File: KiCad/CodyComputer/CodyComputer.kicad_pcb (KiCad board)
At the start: 2 copper layers, 160 x 100 mm, 59 parts, among them J1 Barrel_Jack, J2 Power LED, J3 PropPlug, J4 Video Out, J5 Audio Out, J6 Cody Expansion/Cartridge Port, J7 Keyboard Connector, J8 Joystick 1, J9 Joystick 2, U1 74HC541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

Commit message: Change socket footprints to long pads
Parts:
- U1: footprint Package_DIP:DIP-20_W7.62mm_Socket -> Package_DIP:DIP-20_W7.62mm_Socket_LongPads
- U3, U5, U7: footprint Package_DIP:DIP-40_W15.24mm_Socket -> Package_DIP:DIP-40_W15.24mm_Socket_LongPads
- U4: footprint Package_DIP:DIP-8_W7.62mm_Socket -> Package_DIP:DIP-8_W7.62mm_Socket_LongPads
- U6: footprint Package_DIP:DIP-32_W15.24mm_Socket -> Package_DIP:DIP-32_W15.24mm_Socket_LongPads
- U8: footprint Package_DIP:DIP-16_W7.62mm_Socket -> Package_DIP:DIP-16_W7.62mm_Socket_LongPads

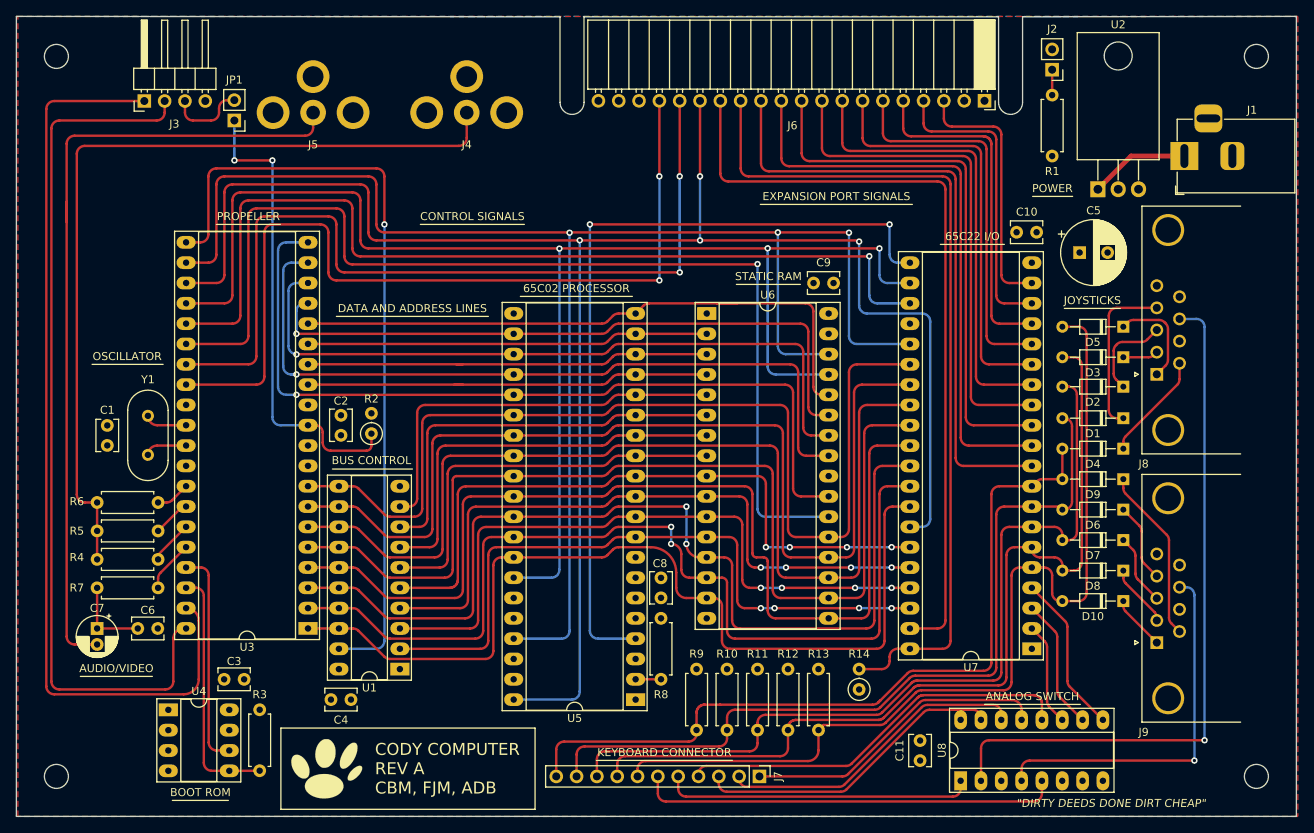
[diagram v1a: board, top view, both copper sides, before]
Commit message: Fix DRC errors for long pads
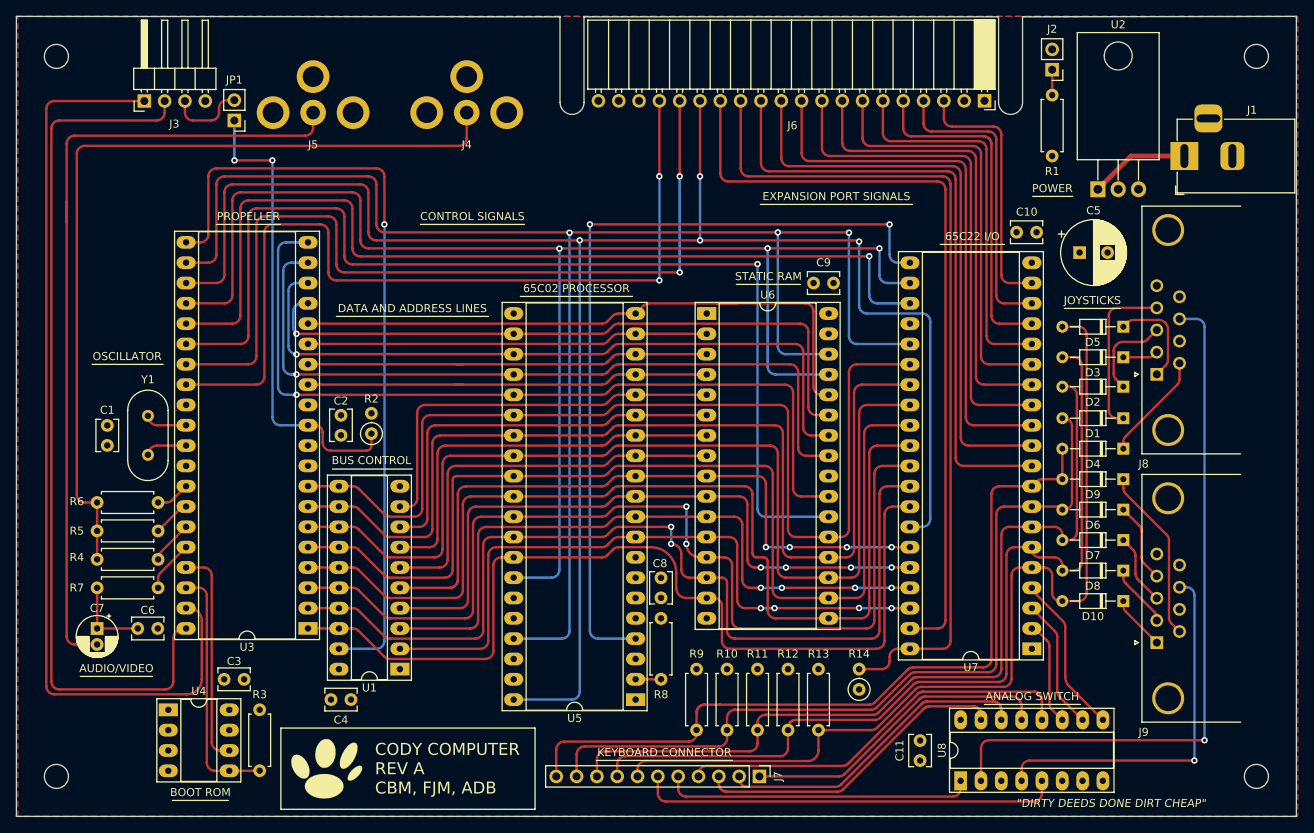
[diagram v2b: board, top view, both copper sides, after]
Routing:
- net /65C22 and IO/COL5: track 99.1 -> 98.5 mm
- net A12: track 82.2 -> 82.7 mm

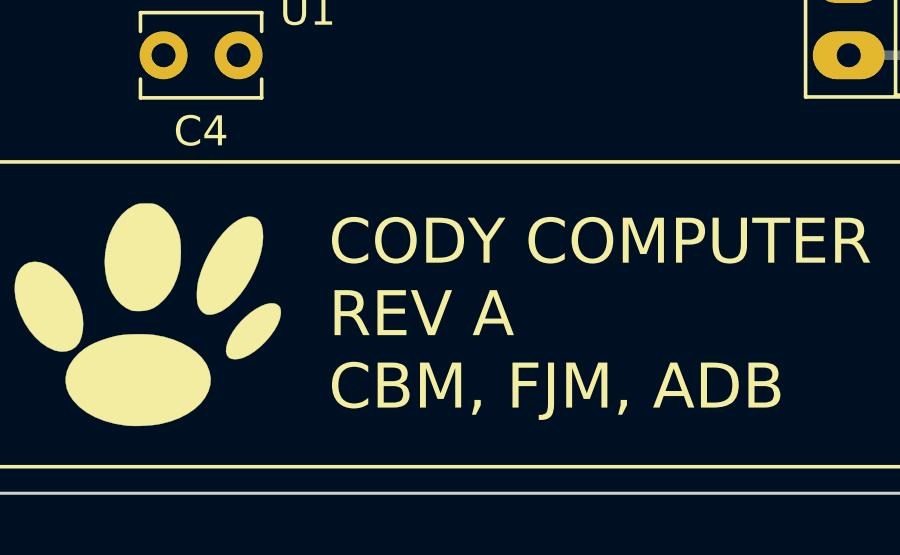
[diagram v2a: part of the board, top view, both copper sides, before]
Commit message: Update board revision to Rev B
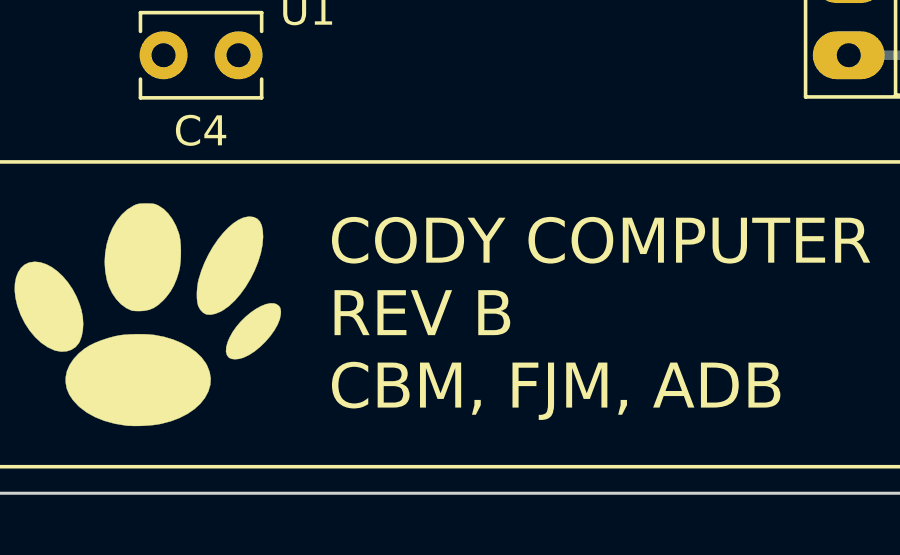
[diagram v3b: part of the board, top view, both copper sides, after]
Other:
- board text added: "CODY COMPUTER REV B CBM, FJM, ADB"
- board text removed: "CODY COMPUTER REV A CBM, FJM, ADB"
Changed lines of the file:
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@@
   (title_block
     (title "Cody Computer Motherboard")
-    (date "2023-04-19")
-    (rev "A")
+    (date "2025-01-06")
+    (rev "B")
   )
   (layers
@@
     (effects (font (size 1 1) (thickness 0.15)))
   )
-  (gr_text "CODY COMPUTER\nREV A\nCBM, FJM, ADB" (at 103.307637 141.346) (layer "F.SilkS")
+  (gr_text "CODY COMPUTER\nREV B\nCBM, FJM, ADB" (at 103.307637 141.346) (layer "F.SilkS")
     (effects (font (size 1.5 1.5) (thickness 0.3)) (justify left))
   )

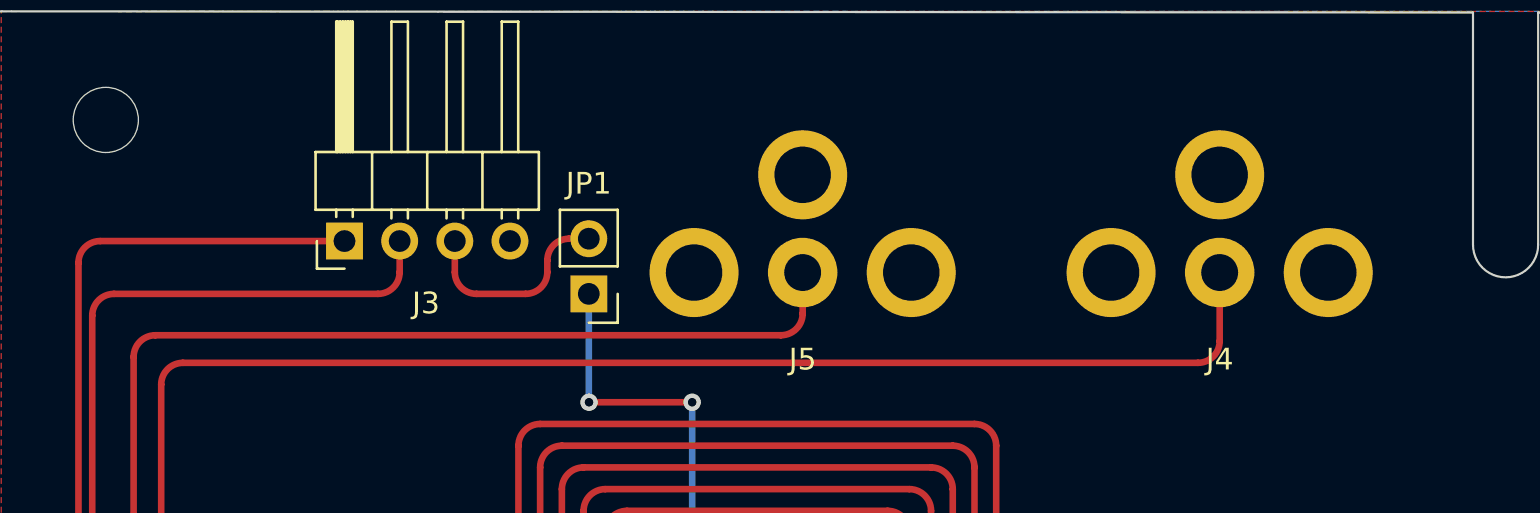
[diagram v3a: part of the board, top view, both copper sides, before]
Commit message: Move RCA connectors 1.7mm for punchout alignment
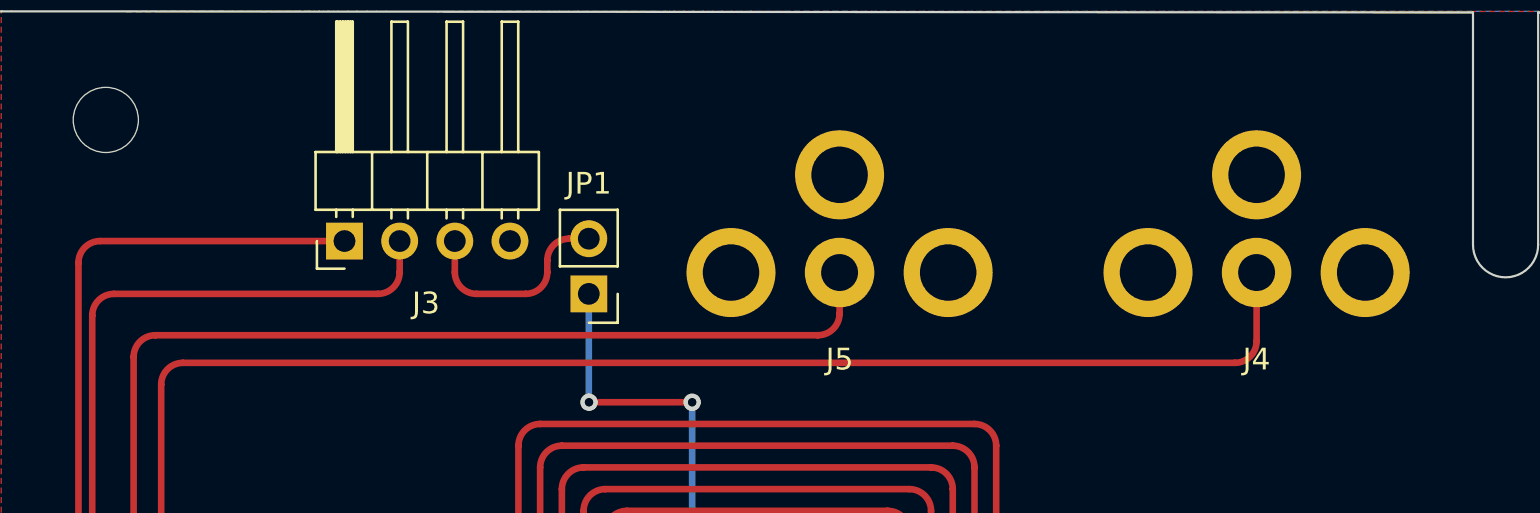
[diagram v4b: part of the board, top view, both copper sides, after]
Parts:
- moved J4 1.70 mm to (116.5, 59.3)
- moved J5 1.70 mm to (97.3, 59.3)
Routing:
- net Net-(C7-Pad2): track 102.2 -> 103.9 mm
- net Net-(J4-Pad1): track 105.7 -> 107.4 mm
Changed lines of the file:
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@@
   )
   (footprint "Cody_Components:CodyRCAJack" (layer "F.Cu")
-    (at 114.78035 59.3378)
+    (at 116.48035 59.3378)
     (descr "RCA audio/video jack modeled after the CUI RCJ-01X part series. Pin numbers are swapped to match KiCad's coaxial connector symbols.")
     (property "Sheetfile" "Propeller.kicad_sch")
@@
   )
   (footprint "Cody_Components:CodyRCAJack" (layer "F.Cu")
-    (at 95.57795 59.3378)
+    (at 97.27795 59.3378)
     (descr "RCA audio/video jack modeled after the CUI RCJ-01X part series. Pin numbers are swapped to match KiCad's coaxial connector symbols.")
     (property "Sheetfile" "Propeller.kicad_sch")
@@
   (segment (start 207.01 137.79) (end 207.01 86.1275) (width 0.3048) (layer "B.Cu") (net 91))
   (arc (start 207.01 86.1275) (mid 206.717107 85.420393) (end 206.01 85.1275) (width 0.3048) (layer "B.Cu") (net 91))
-  (segment (start 114.78035 62.495) (end 114.78035 59.3378) (width 0.3048) (layer "F.Cu") (net 92))
+  (segment (start 67.04 63.495) (end 115.48035 63.495) (width 0.3048) (layer "F.Cu") (net 92))
   (segment (start 68.58 108.072) (end 68.58 115.184) (width 0.3048) (layer "F.Cu") (net 92))
-  (segment (start 67.04 63.495) (end 113.78035 63.495) (width 0.3048) (layer "F.Cu") (net 92))
+  (segment (start 66.04 107.072) (end 66.04 64.495) (width 0.3048) (layer "F.Cu") (net 92))
   (segment (start 68.58 108.072) (end 67.04 108.072) (width 0.3048) (layer "F.Cu") (net 92))
-  (segment (start 66.04 107.072) (end 66.04 64.495) (width 0.3048) (layer "F.Cu") (net 92))
-  (arc (start 113.78035 63.495) (mid 114.487457 63.202107) (end 114.78035 62.495) (width 0.3048) (layer "F.Cu") (net 92))
+  (segment (start 116.48035 62.495) (end 116.48035 59.3378) (width 0.3048) (layer "F.Cu") (net 92))
+  (arc (start 66.04 64.495) (mid 66.332893 63.787893) (end 67.04 63.495) (width 0.3048) (layer "F.Cu") (net 92))
   (arc (start 67.04 108.072) (mid 66.332893 107.779107) (end 66.04 107.072) (width 0.3048) (layer "F.Cu") (net 92))
-  (arc (start 66.04 64.495) (mid 66.332893 63.787893) (end 67.04 63.495) (width 0.3048) (layer "F.Cu") (net 92))
+  (arc (start 115.48035 63.495) (mid 116.187457 63.202107) (end 116.48035 62.495) (width 0.3048) (layer "F.Cu") (net 92))
+  (segment (start 97.27795 61.225) (end 97.27795 59.3378) (width 0.3048) (layer "F.Cu") (net 93))
+  (segment (start 64.77 124.82) (end 64.77 70.48) (width 0.3048) (layer "F.Cu") (net 93))
+  (segment (start 68.58 125.82) (end 65.77 125.82) (width 0.3048) (layer "F.Cu") (net 93))
   (segment (start 64.77 73.02) (end 64.77 63.225) (width 0.3048) (layer "F.Cu") (net 93))
-  (segment (start 95.57795 61.225) (end 95.57795 59.3378) (width 0.3048) (layer "F.Cu") (net 93))
-  (segment (start 64.77 124.82) (end 64.77 70.48) (width 0.3048) (layer "F.Cu") (net 93))
-  (segment (start 65.77 62.225) (end 94.57795 62.225) (width 0.3048) (layer "F.Cu") (net 93))
-  (segment (start 68.58 125.82) (end 65.77 125.82) (width 0.3048) (layer "F.Cu") (net 93))
-  (arc (start 65.77 62.225) (mid 65.062893 62.517893) (end 64.77 63.225) (width 0.3048) (layer "F.Cu") (net 93))
-  (arc (start 95.57795 61.225) (mid 95.285057 61.932107) (end 94.57795 62.225) (width 0.3048) (layer "F.Cu") (net 93))
+  (segment (start 65.77 62.225) (end 96.27795 62.225) (width 0.3048) (layer "F.Cu") (net 93))
+  (arc (start 64.77 63.225) (mid 65.062893 62.517893) (end 65.77 62.225) (width 0.3048) (layer "F.Cu") (net 93))
+  (arc (start 96.27795 62.225) (mid 96.985057 61.932107) (end 97.27795 61.225) (width 0.3048) (layer "F.Cu") (net 93))
   (arc (start 64.77 124.82) (mid 65.062893 125.527107) (end 65.77 125.82) (width 0.3048) (layer "F.Cu") (net 93))
   (segment (start 68.58 118.74) (end 68.58 123.82) (width 0.3048) (layer "F.Cu") (net 94))
